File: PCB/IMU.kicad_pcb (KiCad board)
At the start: 2 copper layers, 68 parts, among them IC1 STM32F405VGT, IC2 ADP3335ARMZ-3.3, IC3 ADP3335ARMZ-5, IC4 MS5611-01BA03, P1 UART1, P2 SWD, P3 UART2, P4 SPI, P5 BATTERY, P6 USB_OTG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

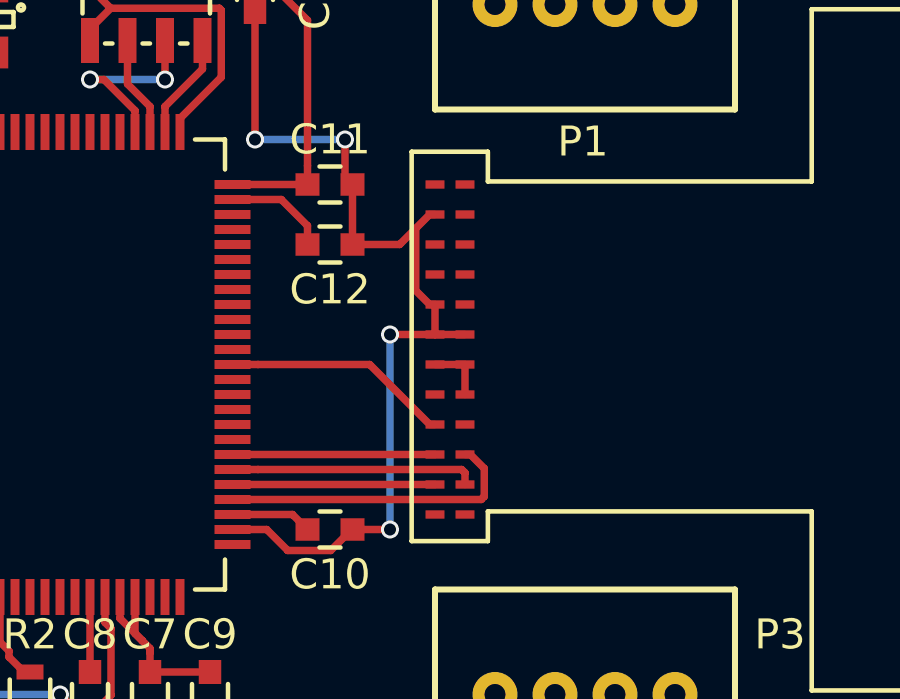
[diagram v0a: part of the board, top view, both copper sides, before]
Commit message: update ADIS16405BMLZ footprint to have bigger pads
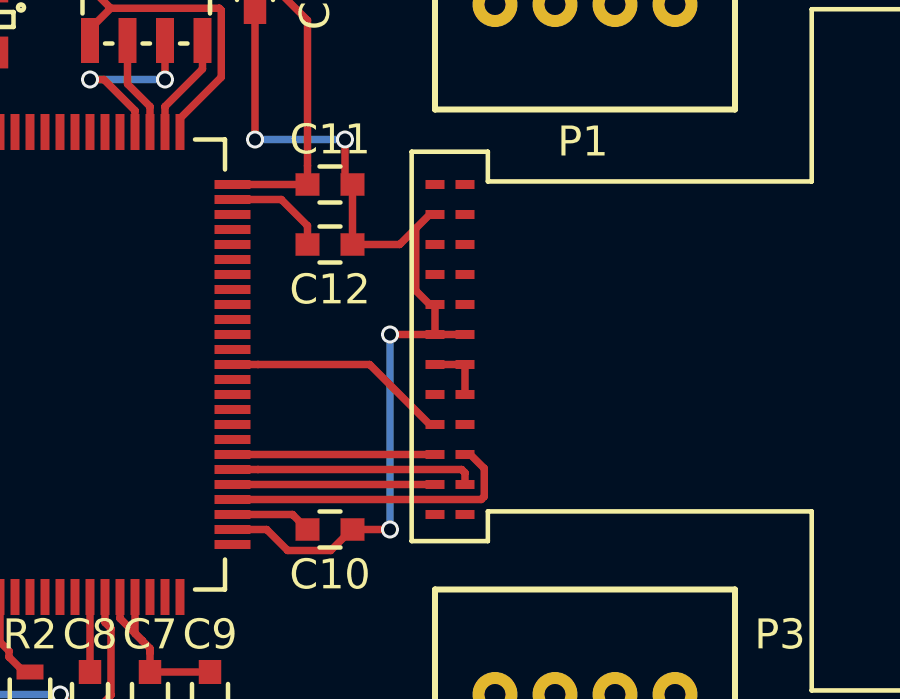
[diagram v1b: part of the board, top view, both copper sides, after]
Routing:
- net (no net): track 0.35 -> 2.35 mm
- net +5V: track 11.7 -> 9.71 mm

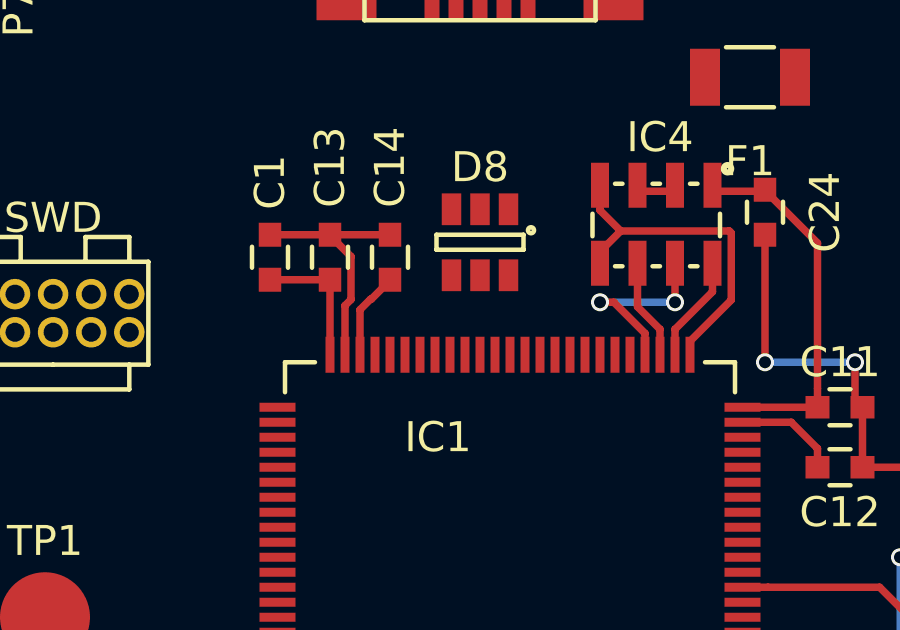
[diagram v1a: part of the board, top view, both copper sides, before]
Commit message: Edit design rules so mimimums are (at least) m2fc values
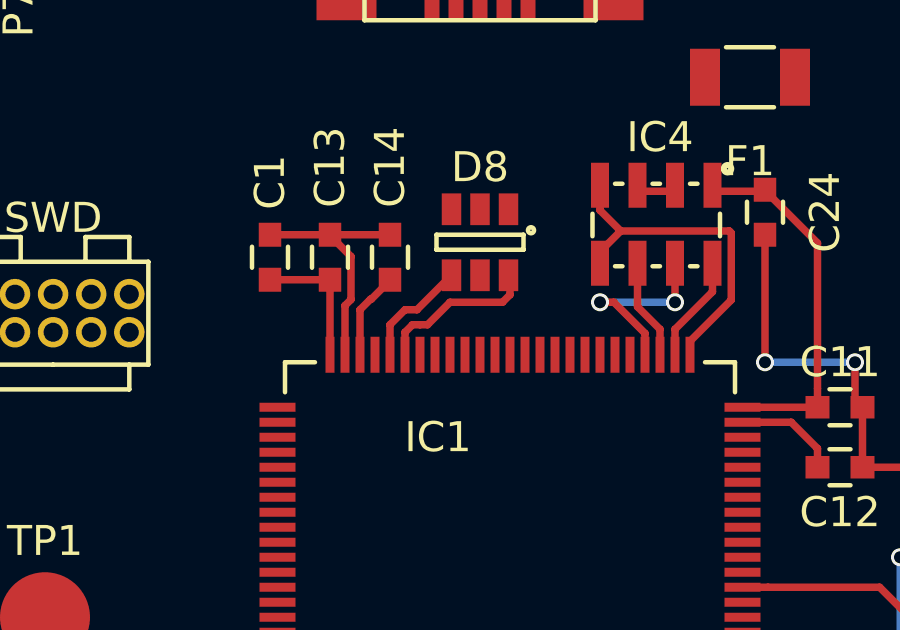
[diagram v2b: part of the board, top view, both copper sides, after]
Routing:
- net OTG_FS_DM: track 0.00 -> 5.44 mm
- net OTG_FS_DP: track 0.00 -> 3.73 mm
- net (no net): track 2.35 -> 0.35 mm
- net +5V: track 9.71 -> 11.7 mm
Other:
- net class Default: via_dia 0.6 -> 0.8
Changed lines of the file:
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@@
   (general
     (links 188)
-    (no_connects 125)
+    (no_connects 112)
     (area 0 0 0 0)
     (thickness 1.6)
     (drawings 0)
-    (tracks 199)
+    (tracks 212)
     (zones 0)
     (modules 68)
@@
     (segment_width 0.2)
     (edge_width 0.1)
-    (via_size 0.6)
+    (via_size 0.8)
     (via_drill 0.4)
     (via_min_size 0.4)
     (via_min_drill 0.3)
-    (uvia_size 0.3)
-    (uvia_drill 0.1)
+    (uvia_size 0.8)
+    (uvia_drill 0.4)
     (uvias_allowed no)
     (uvia_min_size 0.2)
@@
     (mod_text_size 1 1)
     (mod_text_width 0.15)
-    (pad_size 1.5 1.5)
-    (pad_drill 0.6)
+    (pad_size 0.5 0.9)
+    (pad_drill 0)
     (pad_to_mask_clearance 0)
     (aux_axis_origin 0 0)
@@
     (clearance 0.2)
     (trace_width 0.25)
-    (via_dia 0.6)
+    (via_dia 0.8)
     (via_drill 0.4)
-    (uvia_dia 0.3)
-    (uvia_drill 0.1)
+    (uvia_dia 0.8)
+    (uvia_drill 0.4)
     (add_net +3V3)
     (add_net +5V)
@@
   )
   (segment (start 191.75 114.75) (end 192 114.5) (width 0.25) (layer F.Cu) (net 0))
-  (segment (start 196.999998 103.00001) (end 196.999998 104.000008) (width 0.25) (layer F.Cu) (net 0))
-  (segment (start 196 103.00001) (end 196.999998 103.00001) (width 0.25) (layer F.Cu) (net 0))
+  (segment (start 175.5 95.25) (end 175.5 92.75) (width 0.25) (layer F.Cu) (net 1))
+  (segment (start 175.5 92.75) (end 173.5 92.75) (width 0.25) (layer F.Cu) (net 1))
   (segment (start 178 113.25) (end 180.5 113.25) (width 0.25) (layer F.Cu) (net 1))
   (segment (start 190 89.75) (end 190 89.775) (width 0.25) (layer F.Cu) (net 1))
@@
   (segment (start 184.5 110.75) (end 184.5 113.25) (width 0.25) (layer F.Cu) (net 1))
   (segment (start 180.5 110.75) (end 180.5 113.25) (width 0.25) (layer F.Cu) (net 1))
-  (segment (start 175.5 95.25) (end 175.5 92.75) (width 0.25) (layer F.Cu) (net 1))
   (segment (start 173.75 109) (end 171.25 109) (width 0.25) (layer F.Cu) (net 1))
-  (segment (start 175.5 92.75) (end 173.5 92.75) (width 0.25) (layer F.Cu) (net 1))
+  (segment (start 176 95.25) (end 176 93.610002) (width 0.25) (layer F.Cu) (net 2))
+  (segment (start 175.5 91.25) (end 177.5 91.25) (width 0.25) (layer F.Cu) (net 2))
+  (segment (start 176.200001 93.410001) (end 176.200001 91.975001) (width 0.25) (layer F.Cu) (net 2))
+  (segment (start 176.200001 91.975001) (end 175.5 91.275) (width 0.25) (layer F.Cu) (net 2))
+  (segment (start 175.5 91.275) (end 175.5 91.25) (width 0.25) (layer F.Cu) (net 2))
+  (segment (start 175.5 91.25) (end 173.5 91.25) (width 0.25) (layer F.Cu) (net 2))
   (segment (start 183.5 114) (end 179.5 114) (width 0.25) (layer B.Cu) (net 2))
   (segment (start 184.5 114.75) (end 184.25 114.75) (width 0.25) (layer F.Cu) (net 2))
@@
   (segment (start 258 140.75) (end 260 140.75) (width 0.25) (layer F.Cu) (net 2))
   (segment (start 193.25 97) (end 193.25 99) (width 0.25) (layer F.Cu) (net 2))
-  (segment (start 175.5 91.25) (end 177.5 91.25) (width 0.25) (layer F.Cu) (net 2))
   (segment (start 186.5 114.75) (end 184.5 114.75) (width 0.25) (layer F.Cu) (net 2))
   (segment (start 188.5 114.75) (end 186.5 114.75) (width 0.25) (layer F.Cu) (net 2))
@@
   (segment (start 184.5 114.725) (end 184.5 114.75) (width 0.25) (layer F.Cu) (net 2))
   (segment (start 180.5 114.725) (end 180.5 114.75) (width 0.25) (layer F.Cu) (net 2))
-  (segment (start 176 95.25) (end 176 93.610002) (width 0.25) (layer F.Cu) (net 2))
-  (segment (start 176.200001 93.410001) (end 176.200001 91.975001) (width 0.25) (layer F.Cu) (net 2))
   (segment (start 176 93.610002) (end 176.200001 93.410001) (width 0.25) (layer F.Cu) (net 2))
-  (segment (start 176.200001 91.975001) (end 175.5 91.275) (width 0.25) (layer F.Cu) (net 2))
-  (segment (start 175.5 91.275) (end 175.5 91.25) (width 0.25) (layer F.Cu) (net 2))
   (segment (start 173.75 108.5) (end 172.110002 108.5) (width 0.25) (layer F.Cu) (net 2))
   (segment (start 172.110002 108.5) (end 171.910001 108.299999) (width 0.25) (layer F.Cu) (net 2))
@@
   (segment (start 171.910001 108.299999) (end 170.475001 108.299999) (width 0.25) (layer F.Cu) (net 2))
   (segment (start 170.475001 108.299999) (end 169.775 109) (width 0.25) (layer F.Cu) (net 2))
-  (segment (start 175.5 91.25) (end 173.5 91.25) (width 0.25) (layer F.Cu) (net 2))
   (segment (start 180 117.5) (end 181.200001 116.299999) (width 0.25) (layer F.Cu) (net 3))
   (segment (start 181.200001 116.299999) (end 181.200001 112.700001) (width 0.25) (layer F.Cu) (net 3))
@@
   (segment (start 190.875 97.5) (end 191.75 98.375) (width 0.25) (layer F.Cu) (net 6))
   (segment (start 176.5 95.25) (end 176.5 93.75) (width 0.25) (layer F.Cu) (net 7))
+  (segment (start 177.5 92.775) (end 177.5 92.75) (width 0.25) (layer F.Cu) (net 7))
+  (segment (start 176.875 93.4) (end 177.5 92.775) (width 0.25) (layer F.Cu) (net 7))
   (segment (start 176.5 93.75) (end 176.85 93.4) (width 0.25) (layer F.Cu) (net 7))
-  (segment (start 177.5 92.775) (end 177.5 92.75) (width 0.25) (layer F.Cu) (net 7))
   (segment (start 176.85 93.4) (end 176.875 93.4) (width 0.25) (layer F.Cu) (net 7))
-  (segment (start 176.875 93.4) (end 177.5 92.775) (width 0.25) (layer F.Cu) (net 7))
   (segment (start 266.5 140.95) (end 265.825 140.95) (width 0.25) (layer F.Cu) (net 8))
   (segment (start 265.825 140.95) (end 263.775 143) (width 0.25) (layer F.Cu) (net 8))
@@
   (segment (start 247.925 140.35) (end 247.85 140.35) (width 0.25) (layer F.Cu) (net 9))
   (segment (start 247.85 140.35) (end 246.9 140.35) (width 0.25) (layer F.Cu) (net 9))
+  (segment (start 196.999998 103.00001) (end 196.999998 104.000008) (width 0.25) (layer F.Cu) (net 10))
+  (segment (start 196 103.00001) (end 196.999998 103.00001) (width 0.25) (layer F.Cu) (net 10))
   (segment (start 242.5 140.35) (end 243.45 140.35) (width 0.25) (layer F.Cu) (net 10))
   (segment (start 243.525001 141.599999) (end 242.75 142.375) (width 0.25) (layer F.Cu) (net 10))
@@
   (segment (start 246.275 141) (end 244.275 143) (width 0.25) (layer F.Cu) (net 11))
   (segment (start 244.275 143) (end 244.25 143) (width 0.25) (layer F.Cu) (net 11))
+  (segment (start 177.5 95.25) (end 177.5 94.25) (width 0.25) (layer F.Cu) (net 21) (status 400000))
+  (segment (start 178.4 93.75) (end 179.55 92.6) (width 0.25) (layer F.Cu) (net 21) (status 800000))
+  (segment (start 178 93.75) (end 178.4 93.75) (width 0.25) (layer F.Cu) (net 21))
+  (segment (start 177.5 94.25) (end 178 93.75) (width 0.25) (layer F.Cu) (net 21))
+  (segment (start 178 95.25) (end 178 94.5) (width 0.25) (layer F.Cu) (net 22) (status 400000))
+  (segment (start 181.5 93.25) (end 181.5 92.65) (width 0.25) (layer F.Cu) (net 22) (status 800000))
+  (segment (start 181.25 93.5) (end 181.5 93.25) (width 0.25) (layer F.Cu) (net 22))
+  (segment (start 179.5 93.5) (end 181.25 93.5) (width 0.25) (layer F.Cu) (net 22))
+  (segment (start 178.75 94.25) (end 179.5 93.5) (width 0.25) (layer F.Cu) (net 22))
+  (segment (start 178.5 94.25) (end 178.75 94.25) (width 0.25) (layer F.Cu) (net 22))
+  (segment (start 178.25 94.25) (end 178.5 94.25) (width 0.25) (layer F.Cu) (net 22))
+  (segment (start 178 94.5) (end 178.25 94.25) (width 0.25) (layer F.Cu) (net 22))
+  (segment (start 181.5 92.65) (end 181.45 92.6) (width 0.25) (layer F.Cu) (net 22) (status C00000))
   (segment (start 181.5 110.75) (end 181.5 112.25) (width 0.25) (layer F.Cu) (net 31))
   (segment (start 181.5 112.25) (end 181.8 112.55) (width 0.25) (layer F.Cu) (net 31))

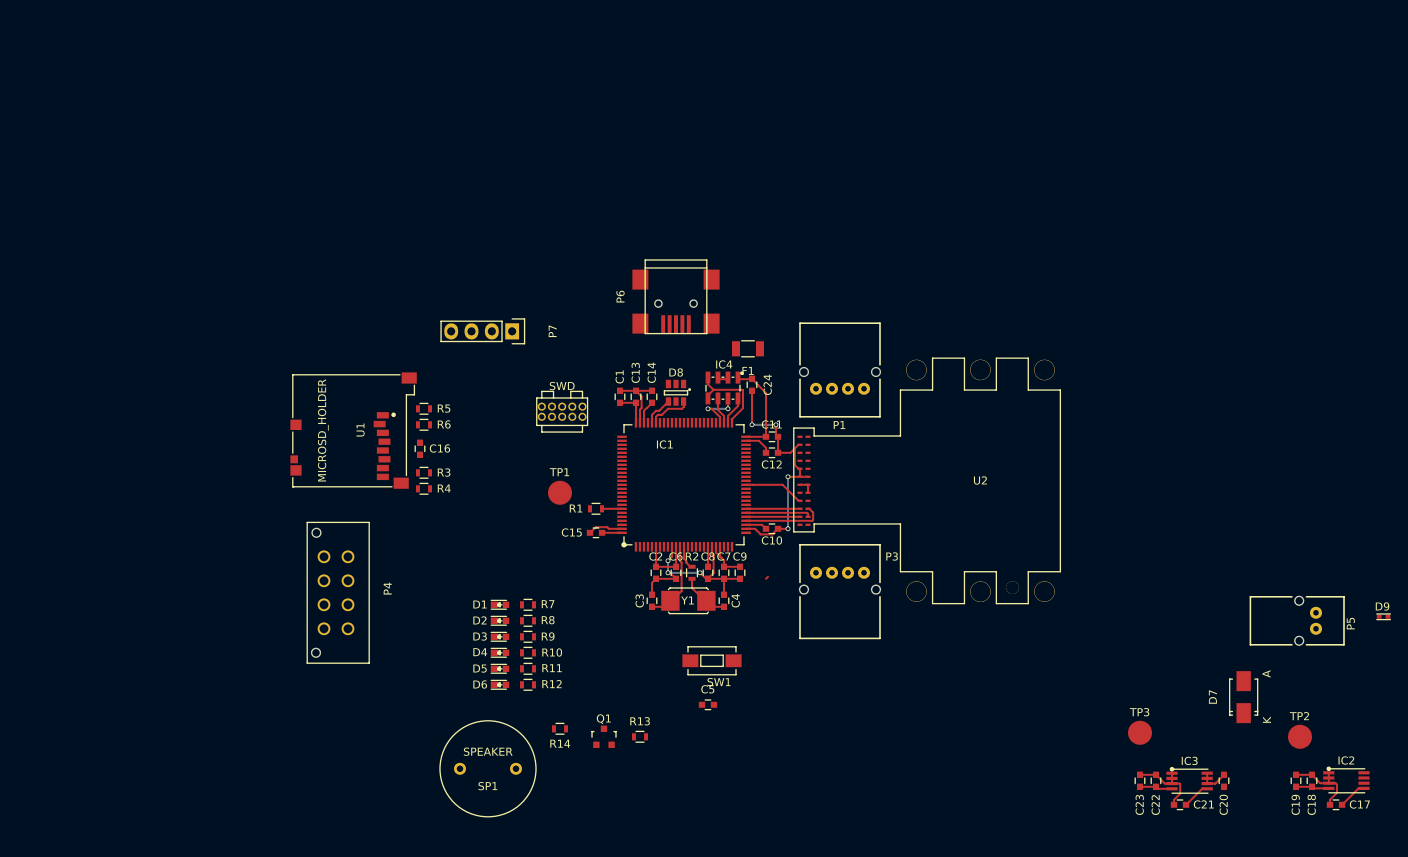
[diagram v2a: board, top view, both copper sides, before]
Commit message: Begin routing near top of microcontroller
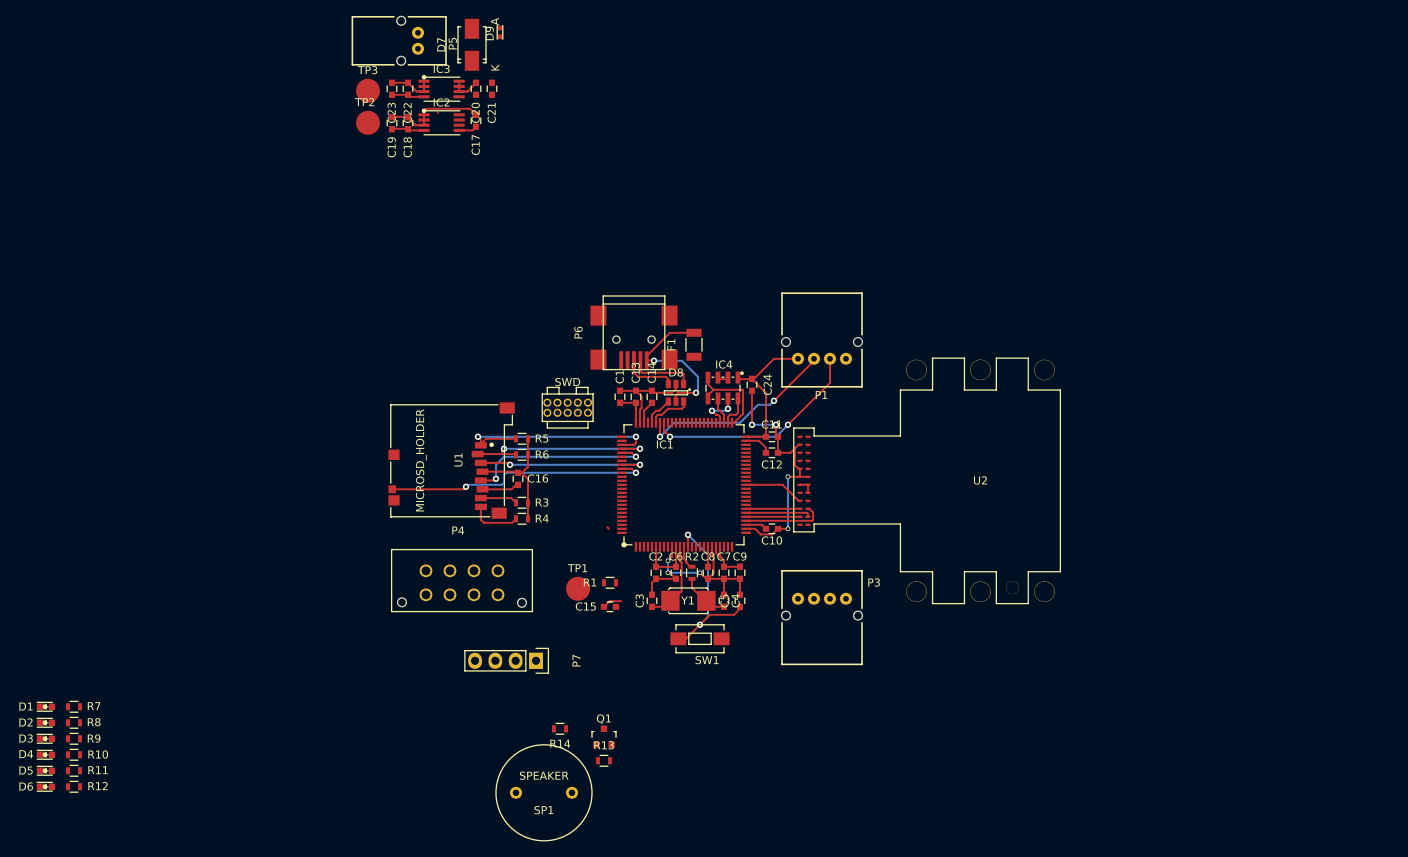
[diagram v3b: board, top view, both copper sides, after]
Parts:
- moved IC2 139.8 mm to (149.0, 56.8)
- moved TP2 139.8 mm to (141.7, 57.8)
- moved C18 139.7 mm to (147.0, 57.8)
- moved C19 139.7 mm to (145.0, 57.8)
- moved C17 137.4 mm to (155.5, 57.5), turned to 270 degrees
- moved P5 133.6 mm to (148.2, 48.5)
- moved D9 131.7 mm to (158.5, 47.0), turned to 90 degrees
- moved C20 127.4 mm to (155.5, 53.5)
- moved C22 127.4 mm to (147.0, 53.5)
- moved C23 127.4 mm to (145.0, 53.5)
- moved IC3 127.4 mm to (149.0, 52.5)
- moved D7 126.3 mm to (155.0, 48.0)
- moved TP3 125.5 mm to (142.0, 53.8)
- moved C21 124.1 mm to (157.5, 53.5), turned to 270 degrees
- moved D1 58.2 mm to (101.8, 130.8)
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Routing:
- net /SDCard/CARD_DETECT: track 0.00 -> 33.9 mm, vias 0 -> 2
- net SDIO_D2: track 0.00 -> 28.4 mm, vias 0 -> 2
- net USART1_TX: track 0.00 -> 27.9 mm, vias 0 -> 2
- net USART1_RX: track 0.00 -> 25.5 mm, vias 0 -> 2
- net SDIO_D3: track 0.00 -> 24.8 mm, vias 0 -> 2
- net +3V3: track 48.5 -> 72.4 mm
- net ~RST: track 0.00 -> 23.7 mm, vias 0 -> 2
- net SDIO_CK: track 0.00 -> 23.6 mm, vias 0 -> 2
- net SDIO_CMD: track 0.00 -> 22.2 mm, vias 0 -> 2
- net /Power/USB5V: track 0.00 -> 20.5 mm, vias 0 -> 2
- net GND: track 80.2 -> 88.9 mm
- net Net-(D8-Pad1): track 0.00 -> 8.12 mm
- net Net-(D8-Pad3): track 0.00 -> 6.78 mm
- net SDIO_D1: track 0.00 -> 6.36 mm
- net SDIO_D0: track 0.00 -> 4.63 mm
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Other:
- net class Power added: clearance 0.2, trace_width 0.3, via_dia 0.8, via_drill 0.4
